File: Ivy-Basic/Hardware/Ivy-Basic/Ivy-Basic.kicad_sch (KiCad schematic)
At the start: 2 parts, among them U1 ESP32-S3-MINI-1, U2 TMC2208-LA

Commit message: I don't know what the diff is here
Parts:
- added C2: 10u, Capacitor_SMD:C_0603_1608Metric, symbol Device:C_Small
- added C3, C4, C5: 100n, symbol Device:C_Small
- added C6: 1u, symbol Device:C_Small
- added C7, C9: 22n, symbol Device:C_Small
- added C8: 4u7, symbol Device:C_Small
- added R4: 10k, symbol Device:R
- added R7, R8: 110m, symbol Device:R
- added R9: 20k, symbol Device:R
- added RV1: R_Potentiometer, symbol Device:R_Potentiometer
- added SW1: SW_Push, symbol Switch:SW_Push
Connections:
- net OB2: now reaches U2.1 (OB2)
- net MS2_1: now reaches U2.10 (MS2)
- net MS2_1: now also U1.6 (IO2)
- net DIAG1: now reaches U2.11 (DIAG)
- net DIAG1: now also U1.11 (IO7)
- net INDEX1: now reaches U2.12 (INDEX)
- net INDEX1: now also U1.12 (IO8)
- net CLK: now reaches U2.13 (CLK)
- net CLK: now also U1.17 (IO13)
- net UART: now reaches U2.14 (PDN_UART)
- net UART: now also U1.16 (IO12)
- net +3V3: now reaches U2.15 (VCC_IO)
- net +3V3: now also U1.3 (3V3), C2.1, C3.1, R4.2
- net STEP1: now reaches U2.16 (STEP)
- net STEP1: now also U1.8 (IO4)
- net at U2.17 (VREF): now also RV1.2
- net GND: now reaches U2.18 (GND), U2.3 (GND)
- net GND: now also U1.1 (GND), U1.2 (GND), U1.42 (GND), U1.43 (GND), U1.46 (GND), U1.47 (GND), U1.48 (GND), U1.49 (GND), U1.50 (GND), U1.51 (GND), U1.52 (GND), U1.53 (GND), U1.54 (GND), U1.55 (GND), U1.56 (GND), U1.57 (GND), U1.58 (GND), U1.59 (GND), U1.60 (GND), U1.61 (GND), U1.62 (GND), U1.63 (GND), U1.64 (GND), U1.65 (GND), C2.2, C3.2, C4.2, C5.2, C6.2, C7.1, C8.1, R7.2, R8.2, RV1.3, SW1.1
- net DIR1: now reaches U2.19 (DIR)
- net DIR1: now also U1.9 (IO5)
- net EN1: now reaches U2.2 (ENN)
- net EN1: now also U1.14 (IO10)
- net OA2: now reaches U2.21 (OA2)
- net VBUS: now reaches U2.22 (VS), U2.28 (VS)
- net VBUS: now also C4.1, C5.1, C6.1
- net at U2.23 (BRA): now also R8.1
- net OA1: now reaches U2.24 (OA1)
- net OB1: now reaches U2.26 (OB1)
- net at U2.27 (BRB): now also R7.1
- net at U2.4 (CPO): now also C9.2
- net at U2.5 (CPI): now also C9.1
- net at U2.6 (VCP): now also C7.2
- net +5V: now reaches U2.8 (5VOUT)
- net +5V: now also C8.2, R9.1
- net MS1_1: now reaches U2.9 (MS1)
- net MS1_1: now also U1.5 (IO1)
- net TX: now reaches U1.39 (TXD0)
- net at U1.4 (IO0): now also SW1.2
- net RX: now reaches U1.40 (RXD0)
- net at U1.45 (EN): now also R4.1
- new net: R9.2, RV1.1
- no-connect marks 0 -> 2
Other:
- note added: "Hard code MS1/MS2? Can at least let the master be user selectable. Does that even make sens?"

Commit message: Replace buck converter with something that might work better
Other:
- note added: "replace this math for 3v3 logic. Or axe it?"
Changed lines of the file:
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@@
+		)
+	)
+	(text "replace this math for 3v3 logic.\nOr axe it?"
+		(exclude_from_sim no)
+		(at 159.766 94.234 0)
+		(effects
+			(font
+				(size 1.27 1.27)
+			)
+			(justify left)
 		)
 	)

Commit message: Add 3D models, set board outline, place USB input, ESP32, Buck Converter
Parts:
- R4: footprint (none) -> Resistor_SMD:R_0402_1005Metric
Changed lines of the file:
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@@
 			)
 		)
-		(property "Footprint" ""
+		(property "Footprint" "Resistor_SMD:R_0402_1005Metric"
 			(at 112.268 33.02 90)
 			(effects

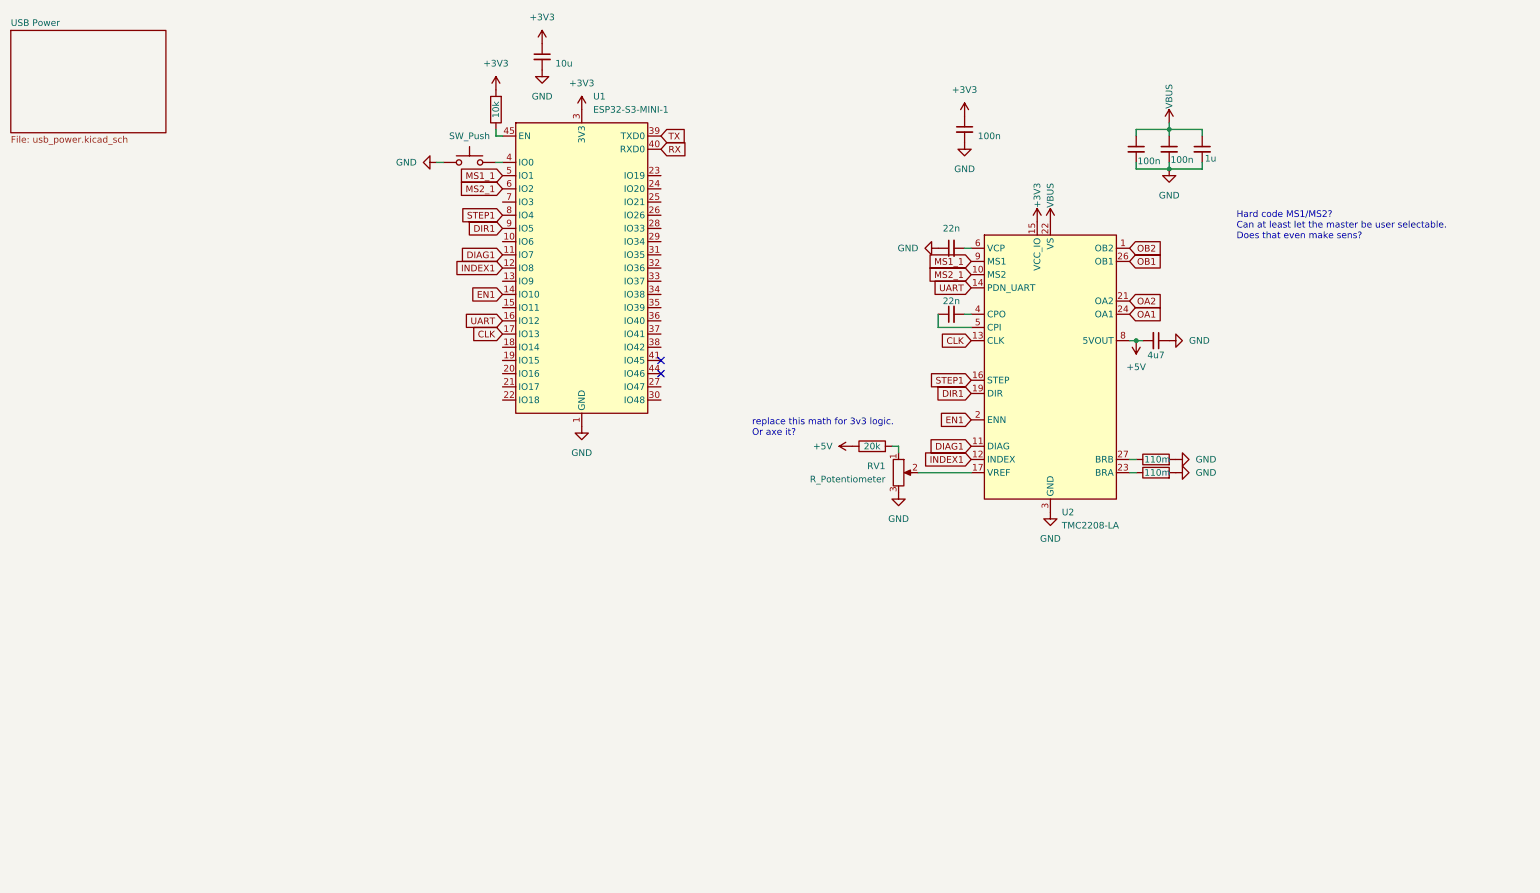
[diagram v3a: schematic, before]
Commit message: add TMC2209
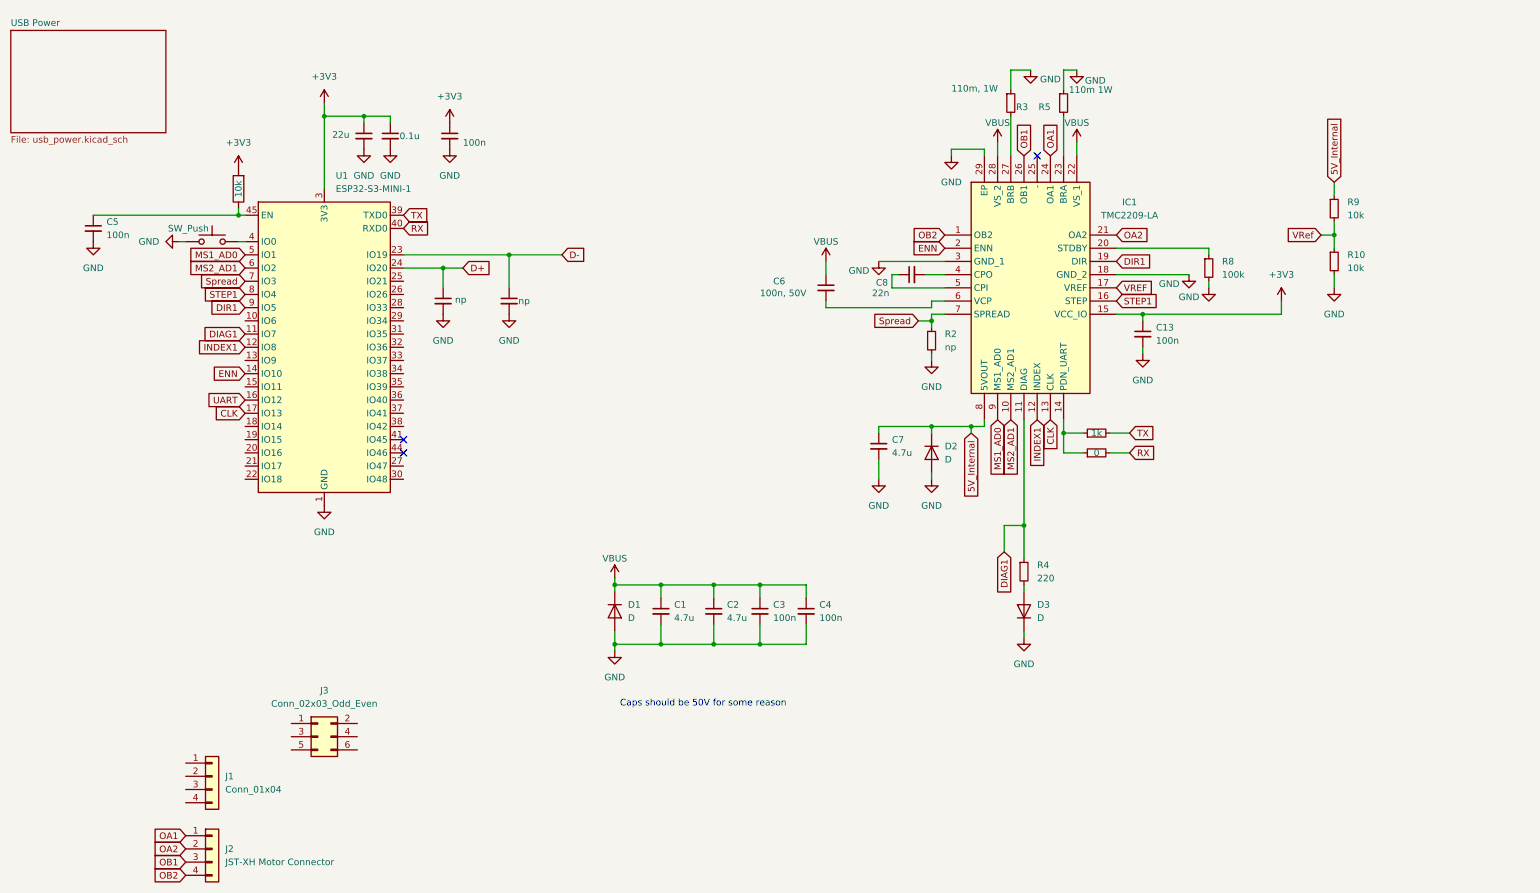
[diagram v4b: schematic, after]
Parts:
- removed C9: 22n, symbol Device:C_Small
- removed R7, R8: 110m, symbol Device:R
- removed R9: 20k, symbol Device:R
- removed RV1: R_Potentiometer, symbol Device:R_Potentiometer
- removed U2: TMC2208-LA, Package_DFN_QFN:TQFN-32-1EP_5x5mm_P0.5mm_EP3.4x3.4mm_ThermalVias, symbol Driver_Motor:TMC2208-LA
- added C1, C2: 4.7u, Capacitor_SMD:C_1206_3216Metric, symbol Device:C_Small
- added C10: 0.1u, Capacitor_SMD:C_0603_1608Metric, symbol Device:C_Small
- added C11, C14: np, Capacitor_SMD:C_0603_1608Metric, symbol Device:C_Small
- added C13: 100n, symbol Device:C_Small
- added C3: 100n, Capacitor_SMD:C_0402_1005Metric, symbol Device:C_Small
- added D1, D2, D3: D, symbol Device:D
- added IC1: TMC2209-LA, QFN50P500X500X90-29N, symbol TMC2209-LA:TMC2209-LA
- added J1: Conn_01x04, symbol Connector_Generic:Conn_01x04
- added J2: JST-XH Motor Connector, symbol Connector_Generic:Conn_01x04
- added J3: Conn_02x03_Odd_Even, symbol Connector_Generic:Conn_02x03_Odd_Even
- added R10, R9: 10k, symbol Device:R_Small
- added R2: np, symbol Device:R_Small
- added R3: 110m, 1W, symbol Device:R_Small
- added R4: 220, symbol Device:R_Small
- added R5: 110m 1W, symbol Device:R_Small
- added R6: 1k, symbol Device:R_Small
- added R7: 0, symbol Device:R_Small
- added R8: 100k, symbol Device:R_Small
- C5: footprint (none) -> Capacitor_SMD:C_0402_1005Metric
- C6: value 1u -> 100n, 50V
- C7: value 22n -> 4.7u
- C8: value 4u7 -> 22n
- C9: renamed from C2; value 10u -> 22u
- renumbered C3 to C12, R4 to R1
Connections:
- net +3V3: now also C10.1, C13.1, IC1.15 (VCC_IO)
- net CLK: now also IC1.13 (CLK)
- net DIAG1: now also IC1.11 (DIAG), R4.1
- net DIR1: now also IC1.19 (DIR)
- net GND: now also C7.2, C1.2, C10.2, C11.2, C13.2, C14.2, C2.2, C3.2, D1.2 (A), D2.2 (A), D3.1 (K), IC1.18 (GND_2), IC1.29 (EP), IC1.3 (GND_1), R10.2, R2.2, R3.1, R5.1, R8.2; no longer C6.2, C7.1, C8.1
- net INDEX1: now also IC1.12 (INDEX)
- net OA1: now also IC1.24 (OA1), J2.1 (Pin_1)
- net OA2: now also IC1.21 (OA2), J2.2 (Pin_2)
- net OB1: now also IC1.26 (OB1), J2.3 (Pin_3)
- net OB2: now also IC1.1 (OB2), J2.4 (Pin_4)
- net RX: now also R7.2
- net STEP1: now also IC1.16 (STEP)
- net TX: now also R6.2
- net VBUS: now also C1.1, C2.1, C3.1, D1.1 (K), IC1.22 (VS_1), IC1.28 (VS_2); no longer C5.1
- net at R1.1, U1.45 (EN): now also C5.1
- net D-: now reaches U1.23 (IO19)
- net D-: now also C14.1
- net D+: now reaches U1.24 (IO20)
- net D+: now also C11.1
- net Spread: now reaches U1.7 (IO3)
- net Spread: now also IC1.7 (SPREAD), R2.1
- net +5V: no longer names the net of C8.2
- net +5V: now also IC1.4 (CPO)
- net EN1 renamed ENN
- net ENN: now also IC1.2 (ENN)
- net MS1_1 renamed MS1_AD0
- net MS1_AD0: now also IC1.9 (MS1_AD0)
- net MS2_1 renamed MS2_AD1
- net MS2_AD1: now also IC1.10 (MS2_AD1)
- new net: IC1.23 (BRA), R5.2
- new net: IC1.14 (PDN_UART), R6.1, R7.1
- new net: C6.2, IC1.6 (VCP)
- new net: D3.2 (A), R4.2
- new net: IC1.20 (STDBY), R8.1
- new net: IC1.27 (BRB), R3.2
- new net: C8.1, IC1.5 (CPI)
- new net 5V_Internal: C7.1, D2.1 (K), IC1.8 (5VOUT), R9.1
- new net VREF: IC1.17 (VREF)
- new net VRef: R10.1, R9.2
- no-connect marks 2 -> 3
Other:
- note added: "Caps should be 50V for some reason"
- note removed: "Hard code MS1/MS2? Can at least let the master be user selectable. Does that even make sens?"
- note removed: "replace this math for 3v3 logic. Or axe it?"
- moved on the sheet: U1
